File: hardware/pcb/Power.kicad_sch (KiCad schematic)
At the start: 17 parts, among them J4 USB_B_Micro, SW1 CSS-1210TB, U3 MCP73831-2-OT, U4 TL431DBZ, U5 TLV73333PDBV

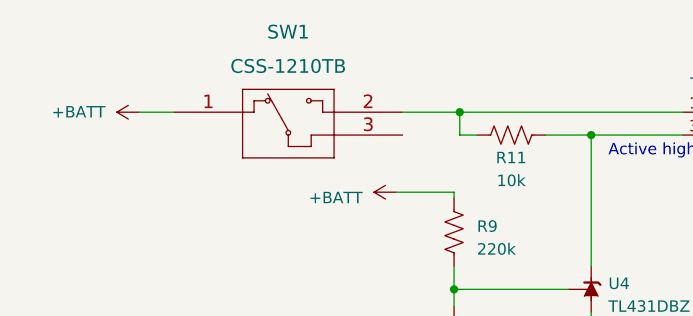
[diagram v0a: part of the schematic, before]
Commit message: Add ESP32 boot button
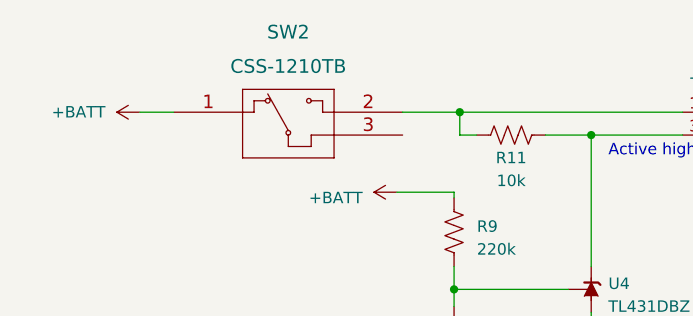
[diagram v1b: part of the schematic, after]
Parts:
- renumbered SW1 to SW2
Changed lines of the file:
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@@
   (symbol (lib_id "CSS-1210TB:CSS-1210TB") (at 34.925 26.67 0) (unit 1)
     (in_bom yes) (on_board yes) (dnp no) (fields_autoplaced)
-    (property "Reference" "SW1" (at 47.625 17.78 0)
+    (property "Reference" "SW2" (at 47.625 17.78 0)
       (effects (font (size 1.524 1.524)))
     )
@@
       (project "Combadge"
         (path "/dc42e7bc-f663-434d-8744-232038ac4fdf/522738f4-f6b2-4897-a079-07da122bd152"
-          (reference "SW1") (unit 1)
+          (reference "SW2") (unit 1)
         )
       )

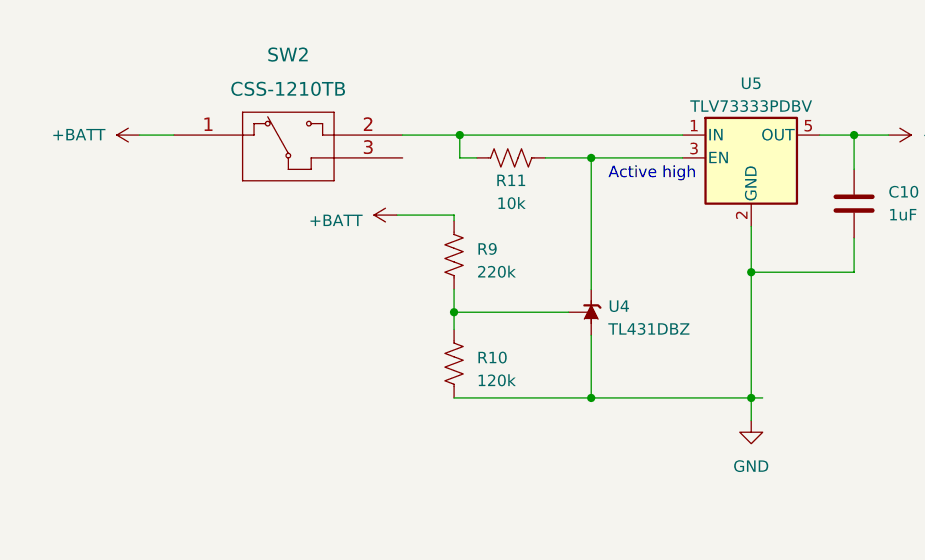
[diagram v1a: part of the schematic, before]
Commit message: Rewire power switch so that the unit can be turned on
Thank you to Reddit user justadiode.
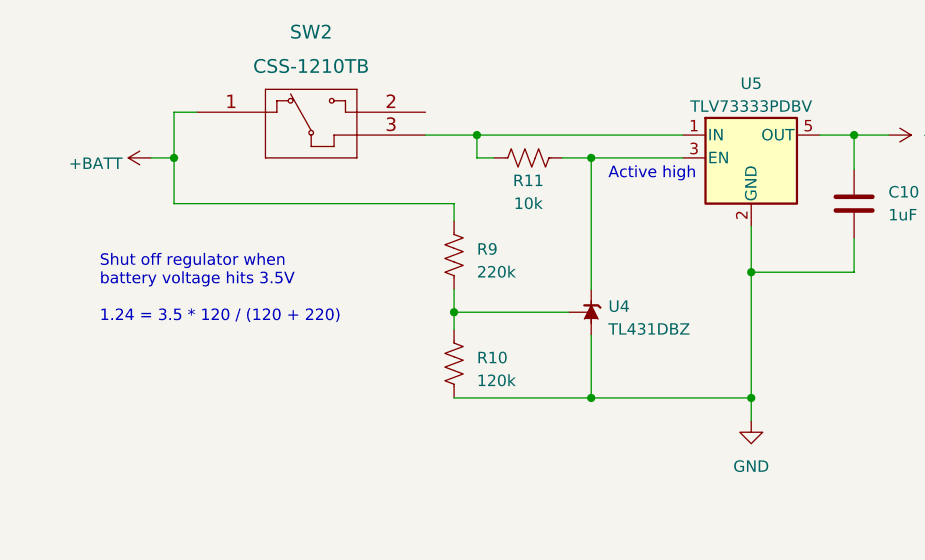
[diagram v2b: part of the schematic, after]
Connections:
- net at R11.1, U5.1 (IN): now also SW2.3; no longer SW2.2
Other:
- note added: "Shut off regulator when battery voltage hits 3.5V 1.24 = 3.5 * 120 / (120 + 220)"
- moved on the sheet: R11, SW2
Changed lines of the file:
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@@
   (junction (at 99.06 41.91) (diameter 0) (color 0 0 0 0)
   )
-  (junction (at 66.675 26.67) (diameter 0) (color 0 0 0 0)
+  (junction (at 68.58 26.67) (diameter 0) (color 0 0 0 0)
   )
   (junction (at 53.34 86.995) (diameter 0) (color 0 0 0 0)
@@
   (junction (at 53.34 113.665) (diameter 0) (color 0 0 0 0)
   )
+  (junction (at 34.925 29.21) (diameter 0) (color 0 0 0 0)
+  )
   (junction (at 48.895 113.665) (diameter 0) (color 0 0 0 0)
   )
@@
   (junction (at 110.49 26.67) (diameter 0) (color 0 0 0 0)
   )
+  (wire (pts (xy 66.04 34.29) (xy 66.04 36.195))
+    (stroke (width 0) (type default))
+  )
+  (wire (pts (xy 68.58 26.67) (xy 91.44 26.67))
+    (stroke (width 0) (type default))
+  )
   (wire (pts (xy 99.06 41.91) (xy 99.06 55.88))
     (stroke (width 0) (type default))
@@
     (stroke (width 0) (type default))
   )
-  (wire (pts (xy 99.06 55.88) (xy 100.33 55.88))
-    (stroke (width 0) (type default))
-  )
-  (wire (pts (xy 31.115 26.67) (xy 34.925 26.67))
-    (stroke (width 0) (type default))
-  )
-  (wire (pts (xy 66.04 36.195) (xy 66.04 35.56))
-    (stroke (width 0) (type default))
-  )
   (wire (pts (xy 64.135 99.06) (xy 64.135 102.87))
     (stroke (width 0) (type default))
@@
     (stroke (width 0) (type default))
   )
+  (wire (pts (xy 37.465 24.13) (xy 34.925 24.13))
+    (stroke (width 0) (type default))
+  )
   (wire (pts (xy 48.895 92.075) (xy 48.895 98.425))
     (stroke (width 0) (type default))
   )
-  (wire (pts (xy 66.04 35.56) (xy 59.69 35.56))
+  (wire (pts (xy 34.925 34.29) (xy 66.04 34.29))
     (stroke (width 0) (type default))
   )
@@
     (stroke (width 0) (type default))
   )
-  (wire (pts (xy 68.58 29.21) (xy 66.675 29.21))
+  (wire (pts (xy 70.485 29.21) (xy 68.58 29.21))
     (stroke (width 0) (type default))
   )
@@
     (stroke (width 0) (type default))
   )
+  (wire (pts (xy 34.925 24.13) (xy 34.925 29.21))
+    (stroke (width 0) (type default))
+  )
   (wire (pts (xy 86.36 124.46) (xy 92.075 124.46))
     (stroke (width 0) (type default))
@@
     (stroke (width 0) (type default))
   )
-  (wire (pts (xy 60.325 26.67) (xy 66.675 26.67))
-    (stroke (width 0) (type default))
-  )
-  (wire (pts (xy 76.2 29.21) (xy 81.28 29.21))
+  (wire (pts (xy 78.105 29.21) (xy 81.28 29.21))
     (stroke (width 0) (type default))
   )
@@
     (stroke (width 0) (type default))
   )
-  (wire (pts (xy 66.675 26.67) (xy 91.44 26.67))
-    (stroke (width 0) (type default))
-  )
   (wire (pts (xy 86.36 99.06) (xy 98.425 99.06))
     (stroke (width 0) (type default))
@@
     (stroke (width 0) (type default))
   )
+  (wire (pts (xy 32.385 29.21) (xy 34.925 29.21))
+    (stroke (width 0) (type default))
+  )
   (wire (pts (xy 32.385 94.615) (xy 35.56 94.615))
     (stroke (width 0) (type default))
@@
     (stroke (width 0) (type default))
   )
+  (wire (pts (xy 62.865 26.67) (xy 68.58 26.67))
+    (stroke (width 0) (type default))
+  )
+  (wire (pts (xy 34.925 34.29) (xy 34.925 29.21))
+    (stroke (width 0) (type default))
+  )
   (wire (pts (xy 110.49 26.67) (xy 110.49 30.48))
     (stroke (width 0) (type default))
@@
     (stroke (width 0) (type default))
   )
-  (wire (pts (xy 66.675 29.21) (xy 66.675 26.67))
-    (stroke (width 0) (type default))
+  (wire (pts (xy 68.58 26.67) (xy 68.58 29.21))
+    (stroke (width 0) (type default))
+  )
+  (text "Shut off regulator when\nbattery voltage hits 3.5V\n\n1.24 = 3.5 * 120 / (120 + 220)"
+    (at 26.67 47.625 0)
+    (effects (font (size 1.27 1.27)) (justify left bottom))
   )
   (text "When R8 is 4k, charge current is 250mA.\n1000/4 = 250, per the datasheet."
@@
     (effects (font (size 1.27 1.27)) (justify left bottom))
   )
-  (symbol (lib_name "+BATT_1") (lib_id "power:+BATT") (at 59.69 35.56 90) (unit 1)
-    (in_bom yes) (on_board yes) (dnp no) (fields_autoplaced)
-    (property "Reference" "#PWR018" (at 63.5 35.56 0)
-      (effects (font (size 1.27 1.27)) hide)
-    )
-    (property "Value" "+BATT" (at 55.88 36.195 90)
-      (effects (font (size 1.27 1.27)) (justify left))
-    )
-    (property "Footprint" "" (at 59.69 35.56 0)
-      (effects (font (size 1.27 1.27)) hide)
-    )
-    (property "Datasheet" "" (at 59.69 35.56 0)
-      (effects (font (size 1.27 1.27)) hide)
-    )
-    (pin "1")
-    (instances
-      (project "Combadge"
-        (path "/dc42e7bc-f663-434d-8744-232038ac4fdf/522738f4-f6b2-4897-a079-07da122bd152"
-          (reference "#PWR018") (unit 1)
-        )
-      )
-    )
-  )
   (symbol (lib_id "power:GND") (at 99.06 58.42 0) (unit 1)
     (in_bom yes) (on_board yes) (dnp no) (fields_autoplaced)
@@
     )
   )
-  (symbol (lib_id "CSS-1210TB:CSS-1210TB") (at 34.925 26.67 0) (unit 1)
-    (in_bom yes) (on_board yes) (dnp no) (fields_autoplaced)
-    (property "Reference" "SW2" (at 47.625 17.78 0)
+  (symbol (lib_id "CSS-1210TB:CSS-1210TB") (at 37.465 24.13 0) (unit 1)
+    (in_bom yes) (on_board yes) (dnp no)
+    (property "Reference" "SW2" (at 50.165 15.24 0)
       (effects (font (size 1.524 1.524)))
     )
-    (property "Value" "CSS-1210TB" (at 47.625 21.59 0)
+    (property "Value" "CSS-1210TB" (at 50.165 19.05 0)
       (effects (font (size 1.524 1.524)))
     )
-    (property "Footprint" "CSS-1210TB:CSS-1210TB" (at 47.625 23.114 0)
+    (property "Footprint" "CSS-1210TB:CSS-1210TB" (at 50.165 20.574 0)
       (effects (font (size 1.524 1.524)) hide)
     )
-    (property "Datasheet" "" (at 34.925 26.67 0)
+    (property "Datasheet" "" (at 37.465 24.13 0)
       (effects (font (size 1.524 1.524)))
     )
@@
     )
   )
-  (symbol (lib_id "Device:R_US") (at 72.39 29.21 90) (unit 1)
+  (symbol (lib_id "Device:R_US") (at 74.295 29.21 90) (unit 1)
     (in_bom yes) (on_board yes) (dnp no)
-    (property "Reference" "R11" (at 72.39 31.75 90)
-      (effects (font (size 1.27 1.27)))
-    )
-    (property "Value" "10k" (at 72.39 34.29 90)
-      (effects (font (size 1.27 1.27)))
-    )
-    (property "Footprint" "Resistor_SMD:R_1206_3216Metric_Pad1.30x1.75mm_HandSolder" (at 72.644 28.194 90)
-      (effects (font (size 1.27 1.27)) hide)
-    )
-    (property "Datasheet" "~" (at 72.39 29.21 0)
+    (property "Reference" "R11" (at 74.295 31.75 90)
+      (effects (font (size 1.27 1.27)))
+    )
+    (property "Value" "10k" (at 74.295 34.29 90)
+      (effects (font (size 1.27 1.27)))
+    )
+    (property "Footprint" "Resistor_SMD:R_1206_3216Metric_Pad1.30x1.75mm_HandSolder" (at 74.549 28.194 90)
+      (effects (font (size 1.27 1.27)) hide)
+    )
+    (property "Datasheet" "~" (at 74.295 29.21 0)
       (effects (font (size 1.27 1.27)) hide)
     )
@@
     )
   )
-  (symbol (lib_id "power:+BATT") (at 31.115 26.67 90) (unit 1)
-    (in_bom yes) (on_board yes) (dnp no)
-    (property "Reference" "#PWR016" (at 34.925 26.67 0)
-      (effects (font (size 1.27 1.27)) hide)
-    )
-    (property "Value" "+BATT" (at 27.305 26.6699 90)
-      (effects (font (size 1.27 1.27)) (justify left))
-    )
-    (property "Footprint" "" (at 31.115 26.67 0)
-      (effects (font (size 1.27 1.27)) hide)
-    )
-    (property "Datasheet" "" (at 31.115 26.67 0)
-      (effects (font (size 1.27 1.27)) hide)
-    )
-    (pin "1")
-    (instances
-      (project "Combadge"
-        (path "/dc42e7bc-f663-434d-8744-232038ac4fdf/522738f4-f6b2-4897-a079-07da122bd152"
-          (reference "#PWR016") (unit 1)
-        )
-      )
-    )
-  )
   (symbol (lib_id "power:+BATT") (at 109.855 113.665 270) (unit 1)
     (in_bom yes) (on_board yes) (dnp no) (fields_autoplaced)
@@
         )
       )
+    )
+  )
+  (symbol (lib_name "+BATT_2") (lib_id "power:+BATT") (at 32.385 29.21 90) (unit 1)
+    (in_bom yes) (on_board yes) (dnp no) (fields_autoplaced)
+    (property "Reference" "#PWR016" (at 36.195 29.21 0)
+      (effects (font (size 1.27 1.27)) hide)
+    )
+    (property "Value" "+BATT" (at 29.21 29.845 90)
+      (effects (font (size 1.27 1.27)) (justify left))
+    )
+    (property "Footprint" "" (at 32.385 29.21 0)
+      (effects (font (size 1.27 1.27)) hide)
+    )
+    (property "Datasheet" "" (at 32.385 29.21 0)
+      (effects (font (size 1.27 1.27)) hide)
+    )
+    (pin "1")
+    (instances
+      (project "Combadge"
+        (path "/dc42e7bc-f663-434d-8744-232038ac4fdf/522738f4-f6b2-4897-a079-07da122bd152"
+          (reference "#PWR016") (unit 1)
+        )
+      )

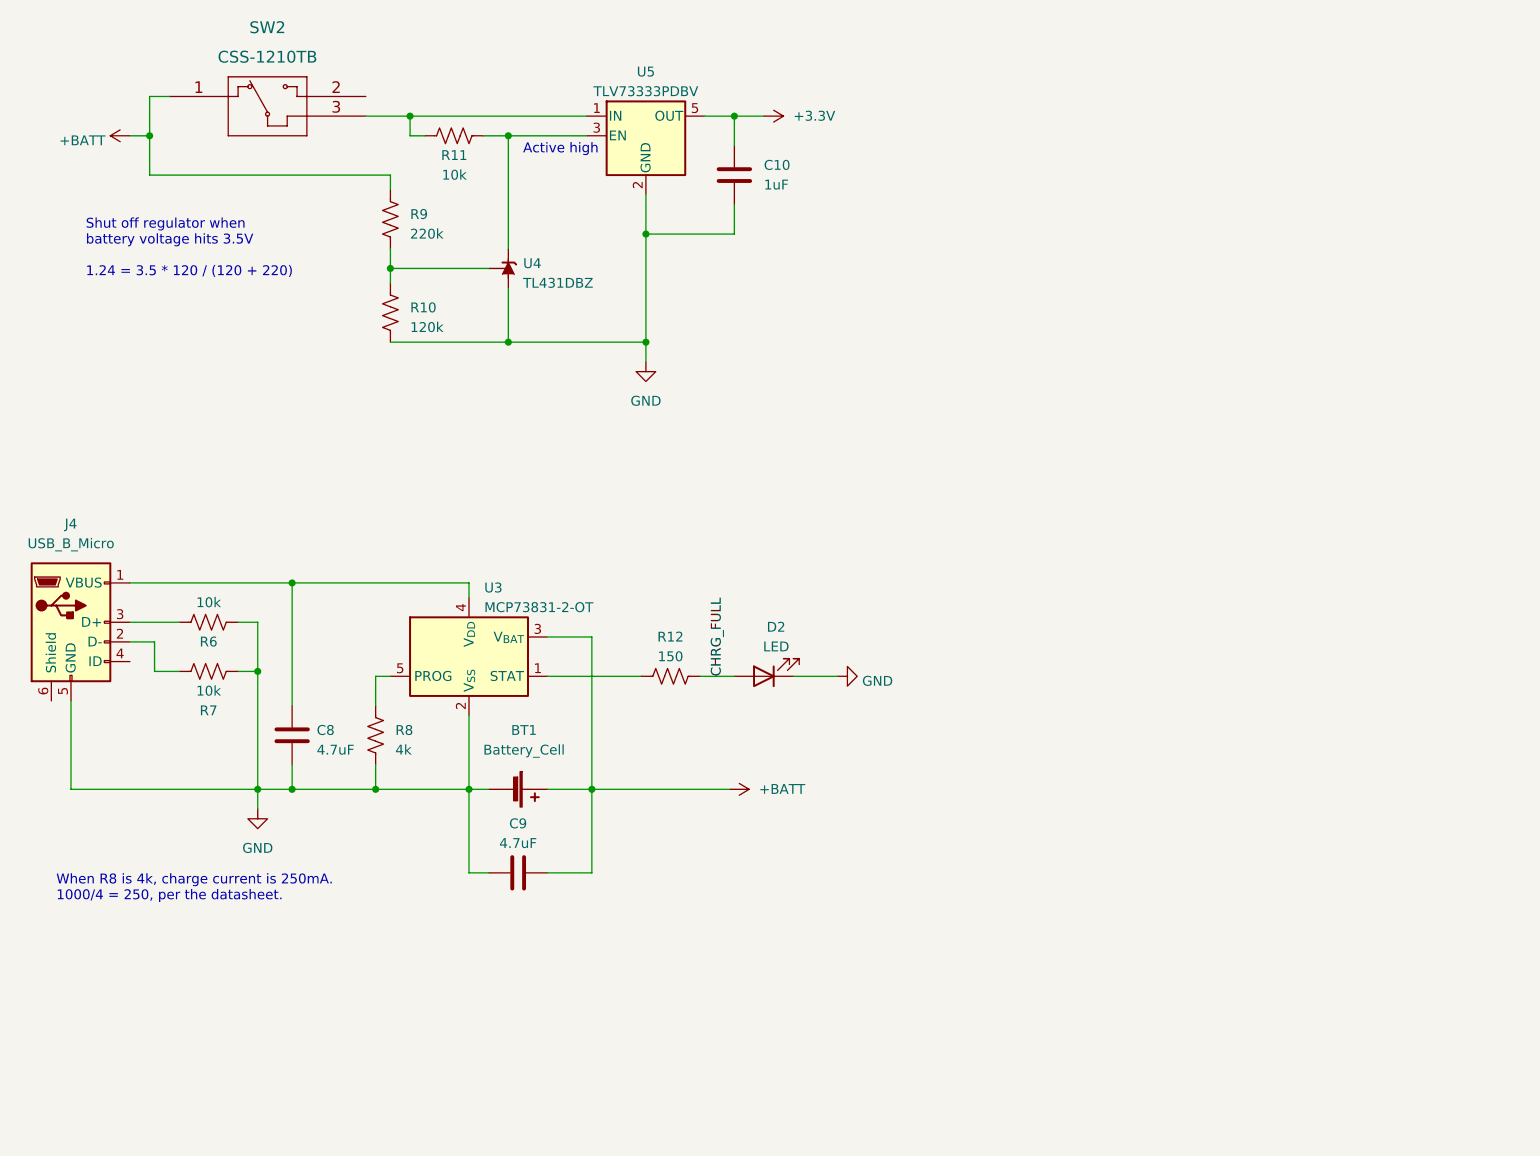
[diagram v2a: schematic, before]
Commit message: Cleanup schematic to follow convention
Thanks to Reddit users Crazy_Direction_1084 and AgentiMi for introducing
me to this.
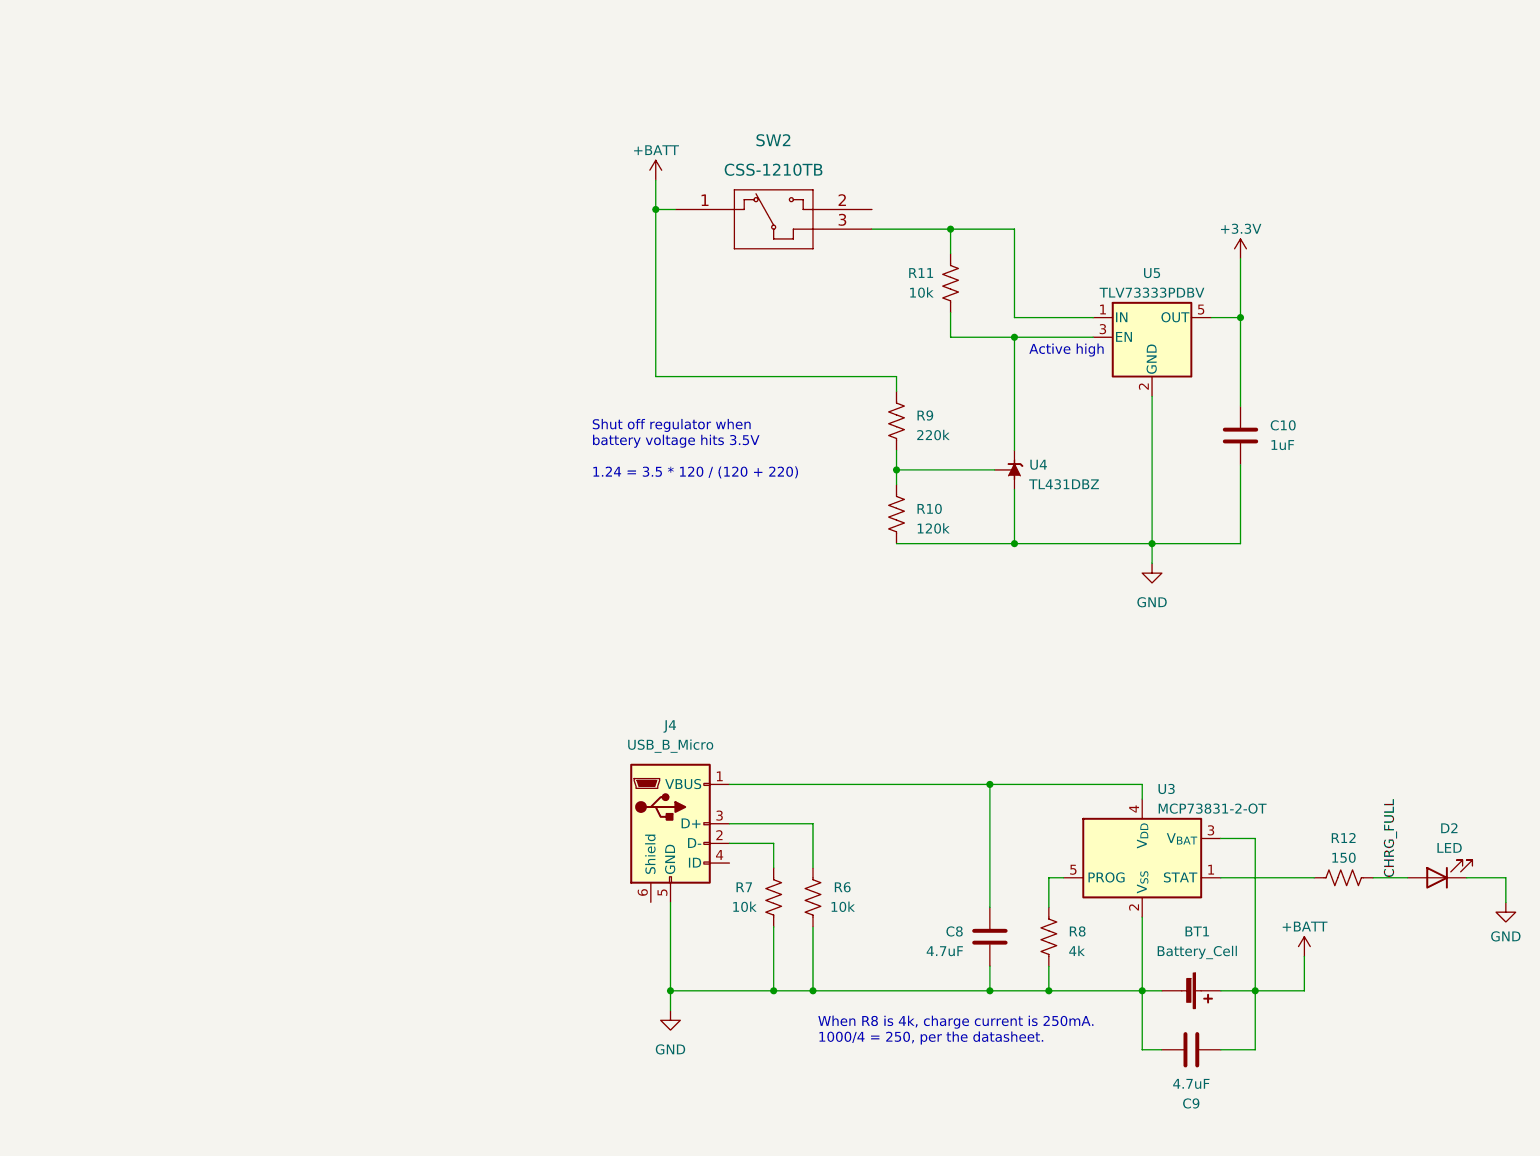
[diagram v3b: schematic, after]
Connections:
- net GND: now also R6.1, R7.1; no longer R6.2, R7.2
- net at J4.2 (D-): now also R7.2; no longer R7.1
- net at J4.3 (D+): now also R6.2; no longer R6.1
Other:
- moved on the sheet: BT1, C10, C8, C9, D2, J4, R10, R11, R12, R6, R7, R8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
